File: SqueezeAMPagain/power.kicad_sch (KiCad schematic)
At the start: 4 parts, among them Q1 Q_NPN_BEC, Q2 PMOS

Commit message: Update .gitignore, L_Radial_D12.0mm_P5+6+7.00mm_Fastron_11P.kicad_mod, SqueezeAMPagain.kicad_pcb, and 13 more files
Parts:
- added C38, C43, C45: 10u/50V, Capacitor_SMD:C_1206_3216Metric, symbol Device:C
- added C42, C44, C50, C57: 100n, Capacitor_SMD:C_0603_1608Metric, symbol Device:C
- added C49: 0.01 μF low ESR, Capacitor_SMD:C_0603_1608Metric, symbol Device:C
- added C51: 150p, Capacitor_SMD:C_0603_1608Metric, symbol Device:C
- added C54: 470u/35V rad, THT, Capacitor_THT:CP_Radial_D8.0mm_P5.00mm, symbol Device:C_Polarized
- added C56: 2.2u/25V, Capacitor_SMD:C_0805_2012Metric, symbol Device:C
- added C58: 2.2u/25V, Capacitor_SMD:C_0603_1608Metric, symbol Device:C
- added C71: 470u, Capacitor_SMD:CP_Elec_6.3x3.9, symbol Device:C_Polarized
- added D2: SS34, Diode_SMD:D_SMA, symbol Device:D_Schottky
- added D3: D_Schottky, Diode_SMD:D_0805_2012Metric, symbol Device:D_Schottky
- added J6: Conn_01x02_Pin, Connector_Phoenix_MC:PhoenixContact_MC_1,5_2-G-3.5_1x02_P3.50mm_Horizontal, symbol Connector:Conn_01x02_Pin
- added J7: Barrel_Jack_Switch_MountingPin, Connector_BarrelJack:BarrelJack_CUI_PJ-079BH_Horizontal, symbol Connector:Barrel_Jack_Switch_MountingPin
- added JP3: RPP, Jumper:SolderJumper-2_P1.3mm_Open_RoundedPad1.0x1.5mm, symbol Jumper:SolderJumper_2_Open
- added JP4: P On, Jumper:SolderJumper-2_P1.3mm_Open_RoundedPad1.0x1.5mm, symbol Jumper:SolderJumper_2_Open
- added JP5: LV On, Jumper:SolderJumper-2_P1.3mm_Open_RoundedPad1.0x1.5mm, symbol Jumper:SolderJumper_2_Open
- added L11: 22uH, Inductor_SMD:L_SXN_SMDRI74, symbol Device:L_Iron
- added L12: 680nH, Inductor_SMD:L_0805_2012Metric, symbol Device:L
- added L8, L9: 4.7uH/3.0A, Inductor:L_Radial_D12.0mm_P5+6+7.00mm_Fastron_11P, symbol Device:L_Iron
- added NT1, NT2: NetTie_2, NetTie:NetTie-2_SMD_Pad2.0mm, symbol Device:NetTie_2
- added Q3, Q7: PMOS, Package_DFN_QFN:Diodes_UDFN2020-6_Type-F, symbol Simulation_SPICE:PMOS
- added Q6: Q_NPN_BEC, Package_TO_SOT_SMD:SOT-23, symbol Device:Q_NPN_BEC
- added R12, R15, R16, R19, R20, R5: 10k, Resistor_SMD:R_0603_1608Metric, symbol Device:R
- added R13: 5.9k, Resistor_SMD:R_0603_1608Metric, symbol Device:R
- added R14: 549R, Resistor_SMD:R_0603_1608Metric, symbol Device:R
- added R17, R18, R4: 150k, Resistor_SMD:R_0603_1608Metric, symbol Device:R
- added U5: TPS5430DDA, Package_SO:TI_SO-PowerPAD-8_ThermalVias, symbol Regulator_Switching:TPS5430DDA
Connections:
- net GND: now also C45.2, C51.2, C54.2, C56.2, C57.2, C58.2, C71.2, D2.2 (A), Q6.2 (E), R13.2, R14.2, R16.2, U5.6 (GND), U5.9 (GNDPAD)
- net LV_ON: now also R15.1
- net PON: now also R2.1
- net ~{WAKE}: now also R19.1
- net at R3.1: now also Q1.1 (B), R2.2
- net at R3.2: now also Q1.2 (E), C38.2, C42.2, NT1.2, NT2.1
- net at Q2.1 (D): now also JP4.2 (B), L9.1
- net at Q2.2 (G): now also Q1.3 (C), R4.2
- net VIN: now reaches Q2.3 (S)
- net VIN: now also C38.1, C42.1, JP4.1 (A), JP5.1 (A), L8.2, Q7.3 (S), R18.1, R4.1
- new net: C45.1, C58.1, L12.2, U5.7 (VIN)
- new net: C50.1, C51.1, R12.2, R13.1, U5.4 (VSENSE)
- new net: C50.2, R14.1
- new net: Q6.1 (B), R15.2, R16.1
- new net: D3.1 (K), Q6.3 (C), Q7.2 (G), R18.2, R19.2
- new net: J6.2 (Pin_2), J7.1, JP3.1 (A), Q3.1 (D), R17.1
- new net: J6.1 (Pin_1), J7.2, NT1.1, R5.2
- new net: JP5.2 (B), L12.1, Q7.1 (D)
- new net: C49.1, U5.1 (BOOT)
- new net: C49.2, D2.1 (K), L11.1, U5.8 (PH)
- new net: Q3.2 (G), R17.2, R5.1
- new net: JP3.2 (B), L8.1, Q3.3 (S)
- new net +3.3V: C54.1, C56.1, C57.1, C71.1, L11.2, R12.1, R20.1
- new net PGND: C43.2, C44.2, NT2.2
- new net PVDD: C43.1, C44.1, L9.2
- new net ~{WAKE_DETECT}: D3.2 (A), R20.2
- no-connect marks 0 -> 1
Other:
- note added: ""Float the pin to enable.""
- note added: "Power Switch"
- note added: "Reverse polarity protection"
- note added: "VGS_max ±20 V!"
- note added: "V_{UVLO,typ} 5.3V"
- moved on the sheet: Q1, Q2, R2, R3

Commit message: Update SqueezeAMPagain.kicad_pcb, SqueezeAMPagain.kicad_prl, USB-Uart.kicad_sch, and 4 more files
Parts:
- removed L12: 680nH, Inductor_SMD:L_0805_2012Metric, symbol Device:L
- added FB5: 600Ω@100MHz 500mA, Inductor_SMD:L_0805_2012Metric, symbol Device:FerriteBead_Small
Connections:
- net at C45.1, C58.1, U5.7 (VIN): now also FB5.2
- net at JP5.2 (B), Q7.1 (D): now also FB5.1
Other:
- moved on the sheet: C45, C49, C50, C51, C54, C58, D2, D3, JP5, L11, Q6, Q7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

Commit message: Update SqueezeAMPagain.kicad_pcb, project.db, power.kicad_sch, and 1 more file
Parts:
- removed C71: 470u, Capacitor_SMD:CP_Elec_6.3x3.9, symbol Device:C_Polarized
- added C2, C6: 100n, Capacitor_SMD:C_0603_1608Metric, symbol Device:C
- added C4: 1n, Capacitor_SMD:C_0603_1608Metric, symbol Device:C
- added C71, C81, C82: 100u, Capacitor_SMD:C_1206_3216Metric, symbol Device:C
- added C8: 220u/10V, Capacitor_THT:CP_Radial_D10.0mm_P2.50mm_P5.00mm, symbol Device:C_Polarized
- C49: value 0.01 μF low ESR -> 10nF 78mOhm
- C54: value 470u/35V rad, THT -> 220u/10V; footprint Capacitor_THT:CP_Radial_D8.0mm_P5.00mm -> Capacitor_THT:CP_Radial_D10.0mm_P2.50mm_P5.00mm; mfr# (none) -> EEUFR1A221; reichelt FR-A 470U 35-3 -> FR-A 220U 10 / FR-A 220U 10B
- C58: footprint Capacitor_SMD:C_0603_1608Metric -> Capacitor_SMD:C_0805_2012Metric
- D2: value SS34 -> SS34 550mV 2A
- L11: value 22uH -> 33uH 120mOhm
- R12: value 10k -> 22k
- R13: value 5.9k -> 13k
- R14: value 549R -> 560R
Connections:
- net +3.3V: now also C2.1, C4.1, C8.1
- net GND: now also C2.2, C6.1, C8.2
- net at C45.1, C58.1, FB5.2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: now also C6.2
- net at C50.1, C51.1, R12.2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: now also C4.2
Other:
- note added: "220uF 35mOhm"
- note added: "TI recommendation: 10k / 5,9k"
- note added: "TI: 549R"
- moved on the sheet: C45, C49, C50, C51, C54, C57, C58, D2, D3, FB5, JP5, L11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

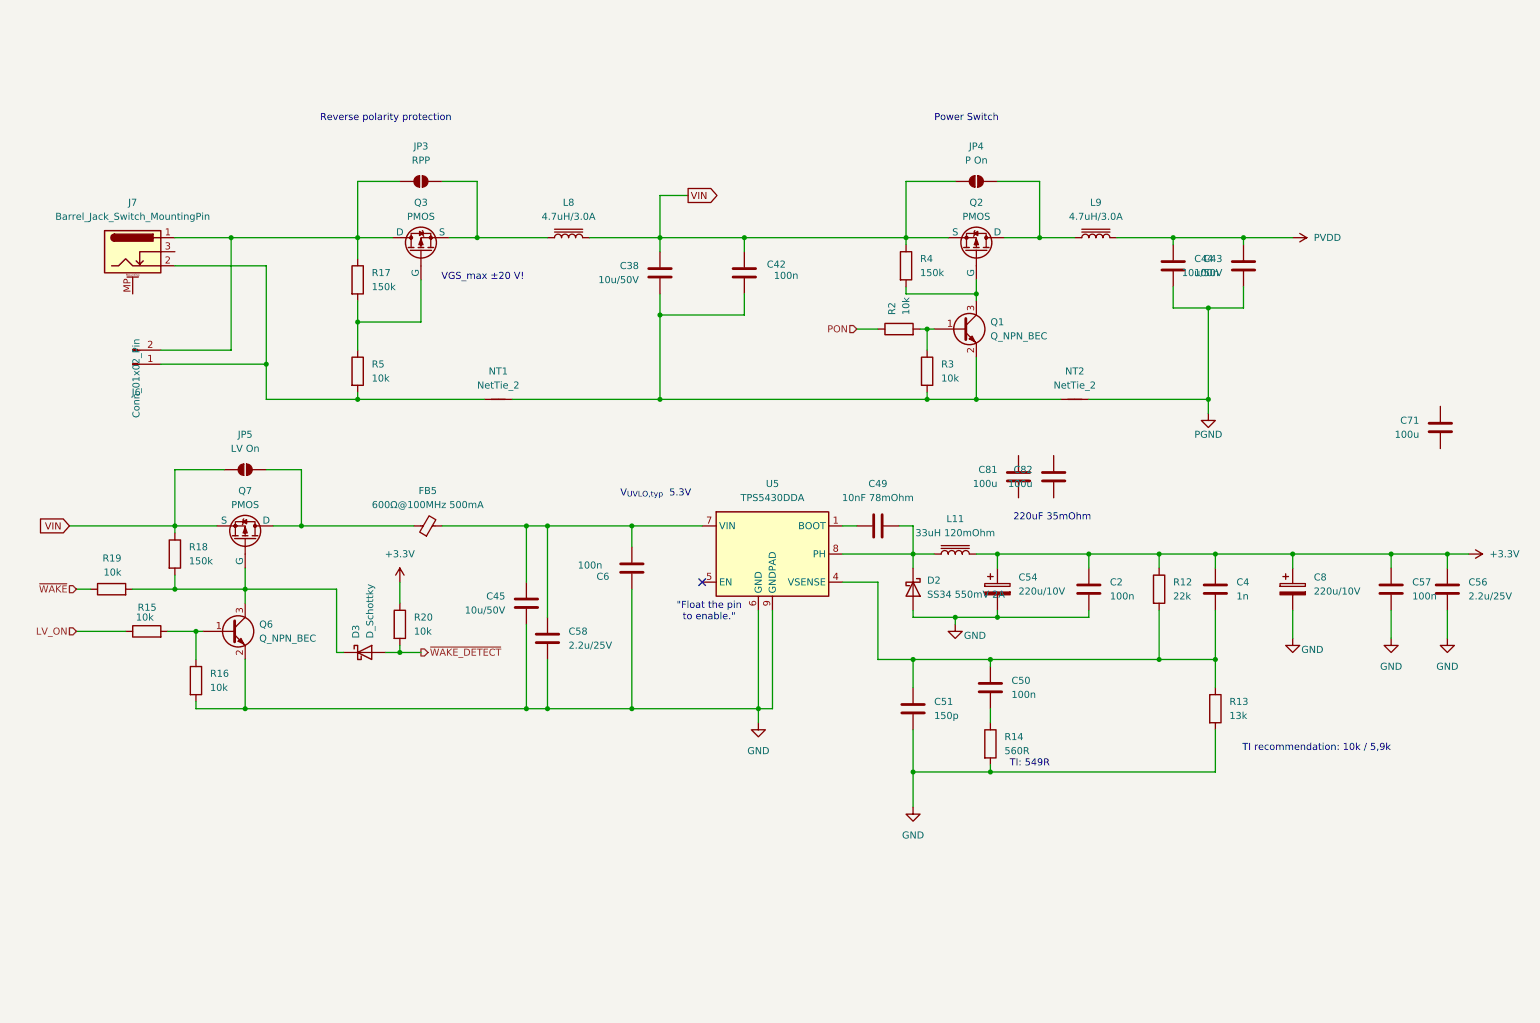
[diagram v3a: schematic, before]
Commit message: Update SqueezeAMPagain.kicad_pcb, SqueezeAMPagain.kicad_sch, USB-Uart.kicad_sch, and 4 more files
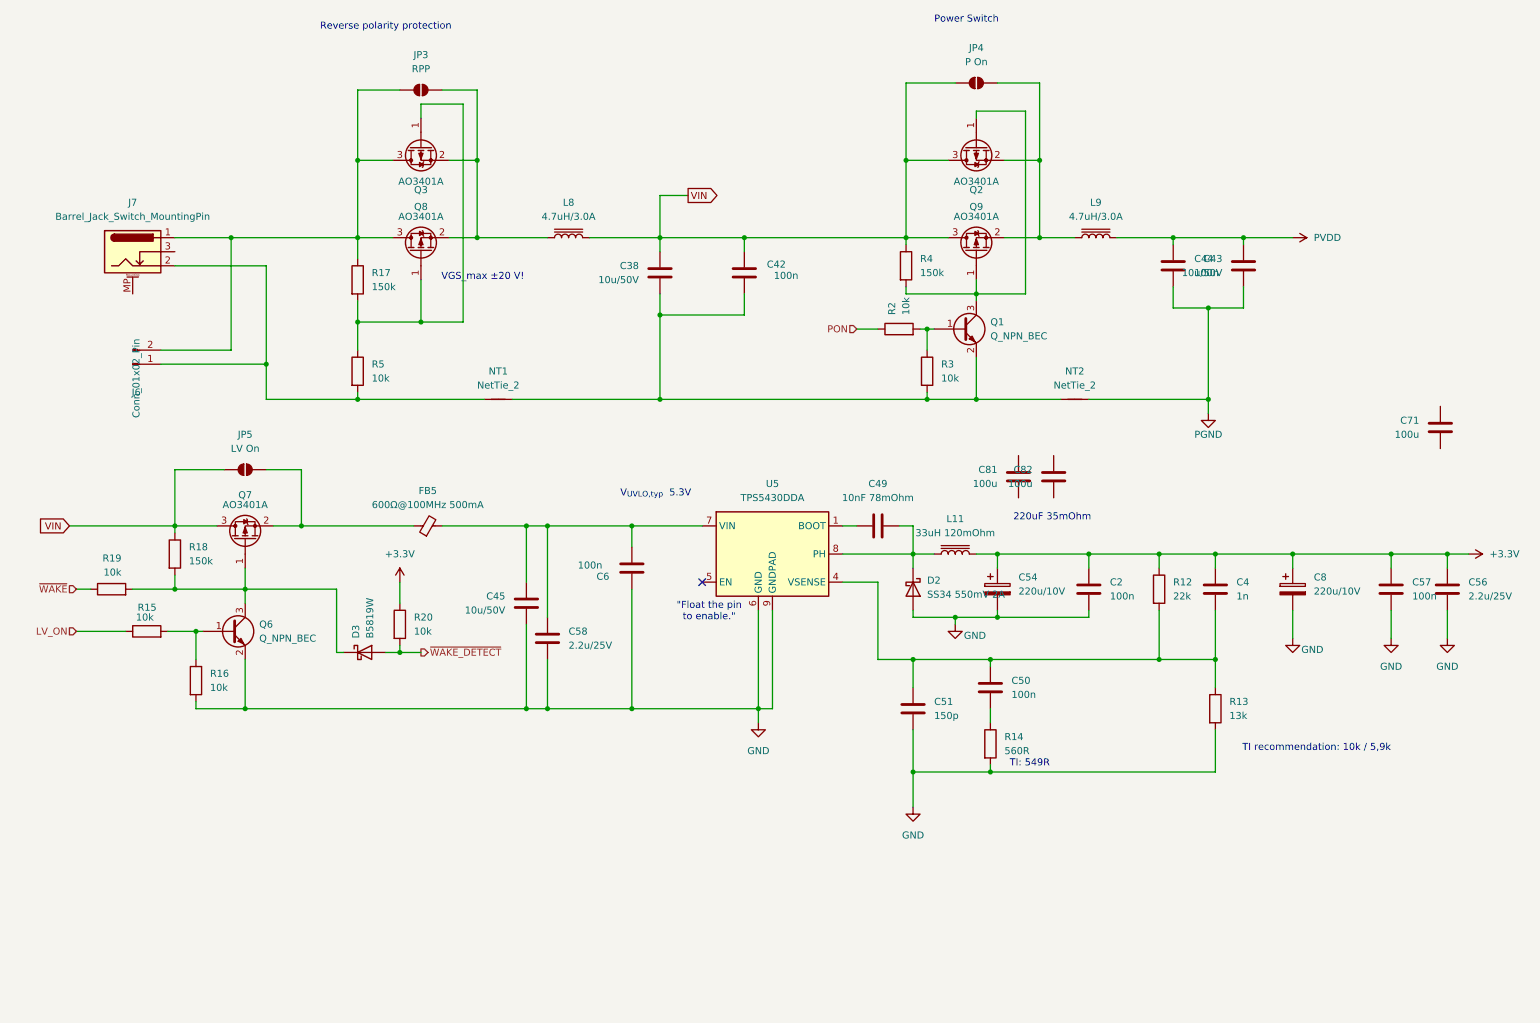
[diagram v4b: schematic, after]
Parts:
- removed Q2, Q3, Q7: PMOS, Package_DFN_QFN:Diodes_UDFN2020-6_Type-F, symbol Simulation_SPICE:PMOS
- added Q2, Q3, Q7, Q8, Q9: AO3401A, Package_TO_SOT_SMD:SOT-23, symbol Transistor_FET:AO3401A
- D3: value D_Schottky -> B5819W; footprint Diode_SMD:D_0805_2012Metric -> Diode_SMD:D_SOD-123; JLCPCB# (none) -> C8598
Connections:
- net VIN: now also Q2.3 (D), Q7.3 (D), Q9.3 (D)
- net at D3.1 (K), Q6.3 (C), R18.2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: now also Q7.1 (G)
- net at J6.2 (Pin_2), J7.1, JP3.1 (A)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: now also Q3.3 (D), Q8.3 (D)
- net at FB5.1, JP5.2 (B): now also Q7.2 (S)
- net at JP4.2 (B), L9.1: now also Q2.2 (S), Q9.2 (S)
- net at Q1.3 (C), R4.2: now also Q2.1 (G), Q9.1 (G)
- net at R17.2, R5.1: now also Q3.1 (G), Q8.1 (G)
- net at JP3.2 (B), L8.1: now also Q3.2 (S), Q8.2 (S)
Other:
- moved on the sheet: JP3, JP4

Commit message: Update SqueezeAMPagain.kicad_pcb, SqueezeAMPagain.kicad_pro, amp.kicad_sch, and 2 more files
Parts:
- removed C54, C8: 220u/10V, Capacitor_THT:CP_Radial_D10.0mm_P2.50mm_P5.00mm, symbol Device:C_Polarized
- removed C71, C81: 100u, Capacitor_SMD:C_1206_3216Metric, symbol Device:C
- removed Q2: AO3401A, Package_TO_SOT_SMD:SOT-23, symbol Transistor_FET:AO3401A
- added C54, C8, C83: 100u / 6.3V, Capacitor_SMD:C_1206_3216Metric, symbol Device:C
- added C59, C60, C61: 10u/50V, Capacitor_SMD:C_1206_3216Metric, symbol Device:C
- added FB1, FB7: 600Ω@100MHz 500mA, Inductor_SMD:L_0805_2012Metric, symbol Device:FerriteBead_Small
- added JP12: SolderJumper_2_Bridged, Jumper:SolderJumper-2_P1.3mm_Bridged2Bar_RoundedPad1.0x1.5mm, symbol Jumper:SolderJumper_2_Bridged
- added Q10: AO3401A, Package_TO_SOT_SMD:SOT-23, symbol Transistor_FET:AO3401A
- C2: value 100n -> 10u/50V; footprint Capacitor_SMD:C_0603_1608Metric -> Capacitor_SMD:C_1206_3216Metric
- C82: value 100u -> 100u / 6.3V; JLCPCB# (none) -> C15008
- L11: footprint Inductor_SMD:L_SXN_SMDRI74 -> Inductor_SMD:L_7.3x7.3_H4.5; mfr PIS2816-220M-04 -> PIS2816-270M-04; reichelt L-PIS2816 22µ -> L-PIS2816 27µ
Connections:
- net +3.3V: now also C82.1, C54.2, C59.1, C60.2, C8.2, C83.1; no longer C2.1
- net GND: now also C2.1, C82.2, C54.1, C59.2, C60.1, C61.2, C8.1, C83.2, FB1.1, JP12.1 (A); no longer C2.2
- net PGND: now also FB1.2, JP12.2 (B)
- net VIN: now also Q3.2 (S), Q9.2 (S), FB7.1; no longer JP5.1 (A), Q7.3 (D), Q9.3 (D), R18.1
- net at C45.1, C58.1, C6.2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: now also C2.2, C61.1
- net at D3.1 (K), Q6.3 (C), R18.2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: now also Q10.1 (G); no longer Q7.1 (G)
- net at Q8.1 (G), R17.2, R5.1: now also Q7.1 (G); no longer Q3.1 (G)
- net at JP3.2 (B), L8.1, Q8.2 (S): now also Q7.2 (S); no longer Q3.2 (S)
- net at J6.2 (Pin_2), J7.1, JP3.1 (A)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: now also Q7.3 (D); no longer Q3.3 (D)
- net at Q1.3 (C), Q9.1 (G), R4.2: now also Q3.1 (G)
- net at JP4.2 (B), L9.1: now also Q3.3 (D), Q9.3 (D); no longer Q9.2 (S)
- net at FB5.1, JP5.2 (B): now also Q10.3 (D); no longer Q7.2 (S)
- net PH: now reaches C49.2, D2.1 (K), L11.1, U5.8 (PH)
- new net: FB7.2, JP5.1 (A), Q10.2 (S), R18.1
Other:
- note removed: "220uF 35mOhm"
- moved on the sheet: C4, C45, C49, C50, C51, C56, C57, C58, C6, D2, D3, FB5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

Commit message: Update SqueezeAMPagain.kicad_pcb, SqueezeAMPagain.kicad_prl, SqueezeAMPagain.kicad_pro, and 6 more files
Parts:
- L8, L9: value 4.7uH/3.0A -> 4.7uH/4.0A; mfr# (none) -> 07HCP-4R7M-50; reichelt# (none) -> L-07HCP 4,7µ
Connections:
- net V_{supply}: now reaches J6.2 (Pin_2), J7.1, JP3.1 (A), Q7.3 (D), Q8.3 (D), R17.1
- net VIN renamed V_{IN}
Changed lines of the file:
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@@
 	)
 	(junction
-		(at 199.39 134.62)
-		(diameter 0)
-		(color 0 0 0 0)
-	)
-	(junction
 		(at 177.8 69.85)
 		(diameter 0)
@@
 	(wire
 		(pts
-			(xy 182.88 134.62) (xy 199.39 134.62)
-		)
-		(stroke
-			(width 0)
-			(type default)
-		)
-	)
-	(wire
-		(pts
 			(xy 177.8 82.55) (xy 186.69 82.55)
 		)
@@
 	(wire
 		(pts
-			(xy 199.39 123.19) (xy 199.39 125.73)
-		)
-		(stroke
-			(width 0)
-			(type default)
-		)
-	)
-	(wire
-		(pts
 			(xy 74.93 146.05) (xy 77.47 146.05)
 		)
@@
 	(wire
 		(pts
-			(xy 199.39 133.35) (xy 199.39 134.62)
-		)
-		(stroke
-			(width 0)
-			(type default)
-		)
-	)
-	(wire
-		(pts
 			(xy 209.55 134.62) (xy 209.55 113.03)
 		)
@@
 	(wire
 		(pts
-			(xy 199.39 134.62) (xy 209.55 134.62)
+			(xy 182.88 134.62) (xy 209.55 134.62)
 		)
 		(stroke
@@
 		)
 	)
-	(global_label "VIN"
+	(label "V_{supply}"
+		(at 58.42 53.34 0)
+		(fields_autoplaced yes)
+		(effects
+			(font
+				(size 1.27 1.27)
+			)
+			(justify left bottom)
+		)
+	)
+	(global_label "V_{IN}"
 		(shape output)
 		(at 134.62 45.72 0)
@@
 		)
 		(property "Intersheetrefs" "${INTERSHEET_REFS}"
-			(at 140.6291 45.72 0)
+			(at 140.2928 45.72 0)
 			(effects
 				(font
@@
 		)
 	)
-	(global_label "VIN"
+	(global_label "V_{IN}"
 		(shape input)
 		(at 22.86 118.11 180)
@@
 		)
 		(property "Intersheetrefs" "${INTERSHEET_REFS}"
-			(at 16.8509 118.11 0)
+			(at 17.1872 118.11 0)
 			(effects
 				(font
@@
 		)
 	)
+	(netclass_flag ""
+		(length 2.54)
+		(shape round)
+		(at 243.84 123.19 0)
+		(fields_autoplaced yes)
+		(effects
+			(font
+				(size 1.27 1.27)
+			)
+			(justify left bottom)
+		)
+		(property "Netclass" "Supply"
+			(at 244.5385 120.65 0)
+			(effects
+				(font
+					(size 1.27 1.27)
+					(italic yes)
+				)
+				(justify left)
+			)
+		)
+	)
+	(netclass_flag ""
+		(length 2.54)
+		(shape round)
+		(at 153.67 53.34 0)
+		(fields_autoplaced yes)
+		(effects
+			(font
+				(size 1.27 1.27)
+			)
+			(justify left bottom)
+		)
+		(property "Netclass" "Supply"
+			(at 154.3685 50.8 0)
+			(effects
+				(font
+					(size 1.27 1.27)
+					(italic yes)
+				)
+				(justify left)
+			)
+		)
+	)
+	(netclass_flag ""
+		(length 2.54)
+		(shape round)
+		(at 41.91 107.95 0)
+		(fields_autoplaced yes)
+		(effects
+			(font
+				(size 1.27 1.27)
+			)
+			(justify left bottom)
+		)
+		(property "Netclass" "Supply"
+			(at 42.6085 105.41 0)
+			(effects
+				(font
+					(size 1.27 1.27)
+					(italic yes)
+				)
+				(justify left)
+			)
+		)
+	)
+	(netclass_flag ""
+		(length 2.54)
+		(shape round)
+		(at 99.06 118.11 0)
+		(fields_autoplaced yes)
+		(effects
+			(font
+				(size 1.27 1.27)
+			)
+			(justify left bottom)
+		)
+		(property "Netclass" "Supply"
+			(at 99.7585 115.57 0)
+			(effects
+				(font
+					(size 1.27 1.27)
+					(italic yes)
+				)
+				(justify left)
+			)
+		)
+	)
+	(netclass_flag ""
+		(length 2.54)
+		(shape round)
+		(at 228.6 53.34 0)
+		(fields_autoplaced yes)
+		(effects
+			(font
+				(size 1.27 1.27)
+			)
+			(justify left bottom)
+		)
+		(property "Netclass" "Supply"
+			(at 229.2985 50.8 0)
+			(effects
+				(font
+					(size 1.27 1.27)
+					(italic yes)
+				)
+				(justify left)
+			)
+		)
+	)
+	(netclass_flag ""
+		(length 2.54)
+		(shape round)
+		(at 48.26 53.34 0)
+		(fields_autoplaced yes)
+		(effects
+			(font
+				(size 1.27 1.27)
+			)
+			(justify left bottom)
+		)
+		(property "Netclass" "Supply"
+			(at 48.9585 50.8 0)
+			(effects
+				(font
+					(size 1.27 1.27)
+					(italic yes)
+				)
+				(justify left)
+			)
+		)
+	)
 	(symbol
 		(lib_id "power:GND")
@@
 			)
 		)
-		(property "Value" "4.7uH/3.0A"
+		(property "Value" "4.7uH/4.0A"
 			(at 113.03 49.53 90)
 			(effects
@@
 			)
 		)
+		(property "reichelt#" "L-07HCP 4,7µ"
+			(at 113.03 53.34 90)
+			(effects
+				(font
+					(size 1.27 1.27)
+				)
+				(hide yes)
+			)
+		)
+		(property "mfr#" "07HCP-4R7M-50"
+			(at 113.03 53.34 90)
+			(effects
+				(font
+					(size 1.27 1.27)
+				)
+				(hide yes)
+			)
+		)
 		(pin "2"
 		)
@@
 			)
 		)
-		(property "Value" "4.7uH/3.0A"
+		(property "Value" "4.7uH/4.0A"
 			(at 208.28 49.53 90)
 			(effects
@@
 			(effects
 				(font
+					(size 1.27 1.27)
+				)
+				(hide yes)
+			)
+		)
+		(property "reichelt#" "L-07HCP 4,7µ"
+			(at 208.28 53.34 90)
+			(effects
+				(font
+					(size 1.27 1.27)
+				)
+				(hide yes)
+			)
+		)
+		(property "mfr#" "07HCP-4R7M-50"
+			(at 208.28 53.34 90)
+			(effects
+				(font

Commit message: Update SqueezeAMPagain.kicad_pcb, SqueezeAMPagain.kicad_prl, SqueezeAMPagain.kicad_pro, and 7 more files
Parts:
- added C71, C81: 100n, Capacitor_SMD:C_0603_1608Metric, symbol Device:C
- added C76: 2.2u/25V, Capacitor_SMD:C_0805_2012Metric, symbol Device:C
- added FB2: 600Ω@100MHz 500mA, Inductor_SMD:L_0805_2012Metric, symbol Device:FerriteBead_Small
- added U7: AMS1117-3.3, Package_TO_SOT_SMD:SOT-223-3_TabPin2, symbol Regulator_Linear:AMS1117-3.3
- C54, C8, C82, C83: value 100u / 6.3V -> 47uF / 10V; JLCPCB# C15008 -> C96123
- C59, C60: value 10u/50V -> 47uF / 10V; JLCPCB# (none) -> C96123
- L11: footprint Inductor_SMD:L_7.3x7.3_H4.5 -> Inductor:L_Vishay_IHLP-3232
- R12: value 22k -> 15k; JLCPCB# (none) -> C22809
- R13: value 13k -> 4.7k; JLCPCB# (none) -> C23162
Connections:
- net +3.3V: now also C71.1, U7.2 (VO); no longer C4.1, C54.2, C56.1, C57.1, C59.1, C60.2, C8.2, C82.1, C83.1, L11.2, R12.1
- net GND: now also C71.2, C76.2, C81.2, U7.1 (GND)
- new net: C76.1, C81.1, FB2.2, U7.3 (VI)
- new net +5V: C4.1, C54.2, C56.1, C57.1, C59.1, C60.2, C8.2, C82.1, C83.1, FB2.1, L11.2, R12.1
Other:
- note removed: "TI recommendation: 10k / 5,9k"

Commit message: Update L_Radial_D12.0mm_P5+6+7.00mm_Fastron_11P.kicad_mod, SqueezeAMPagain.kicad_pcb, SqueezeAMPagain.kicad_prl, and 5 more files
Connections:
- net GND_{IN}: now reaches C38.2, C42.2, NT1.2, NT2.1, Q1.2 (E), R3.2
- net V_{IN,SW}: now reaches JP4.2 (B), L9.1, Q3.3 (D), Q9.3 (D)
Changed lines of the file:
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@@
+		)
+	)
+	(label "V_{IN,SW}"
+		(at 193.04 25.4 0)
+		(fields_autoplaced yes)
+		(effects
+			(font
+				(size 1.27 1.27)
+			)
+			(justify left bottom)
+		)
+	)
+	(label "GND_{IN}"
+		(at 138.43 82.55 0)
+		(fields_autoplaced yes)
+		(effects
+			(font
+				(size 1.27 1.27)
+			)
+			(justify left bottom)
 		)
 	)
@@
 			(effects
 				(font
+					(size 1.27 1.27)
+					(italic yes)
+				)
+				(justify left)
+			)
+		)
+	)
+	(netclass_flag ""
+		(length 2.54)
+		(shape round)
+		(at 64.77 107.95 0)
+		(fields_autoplaced yes)
+		(effects
+			(font
+				(size 1.27 1.27)
+			)
+			(justify left bottom)
+		)
+		(property "Netclass" "Supply"
+			(at 65.4685 105.41 0)
+			(effects
+				(font
